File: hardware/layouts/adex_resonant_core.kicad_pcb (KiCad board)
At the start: 4 copper layers, 50 x 50 mm, 96 parts

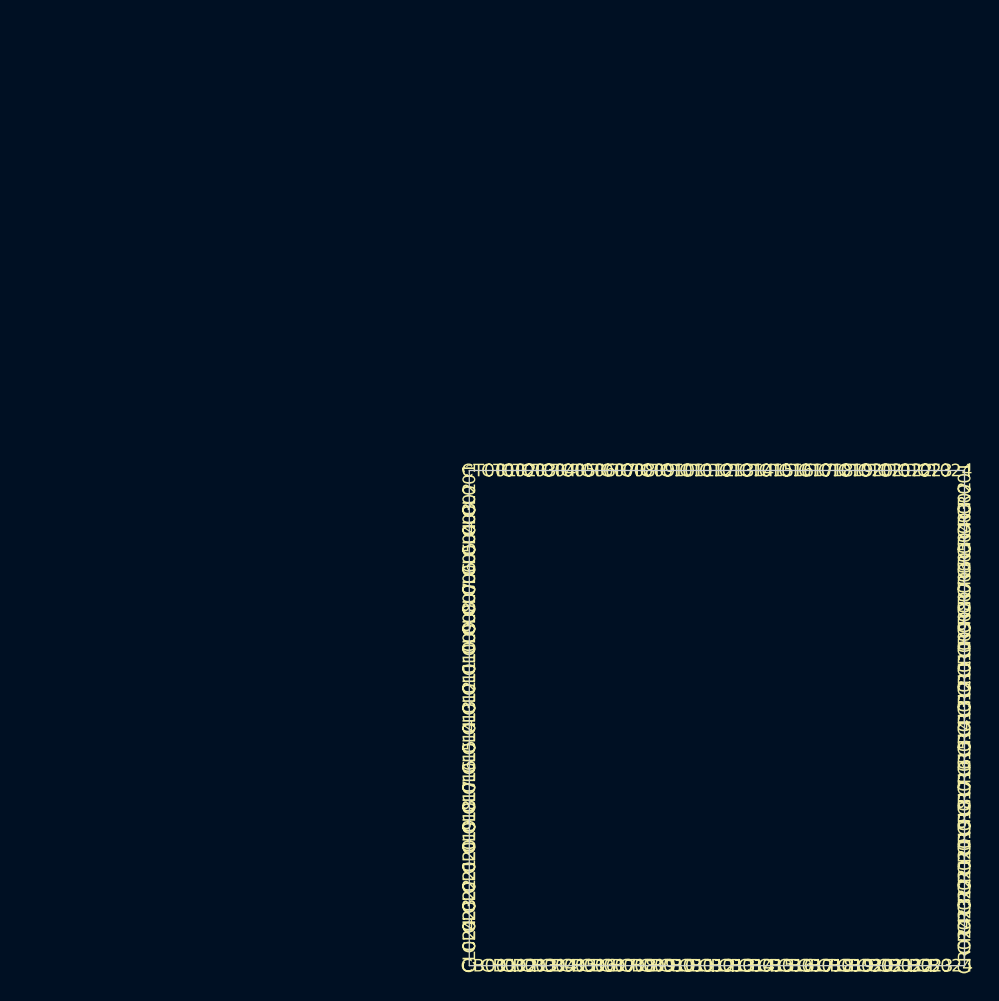
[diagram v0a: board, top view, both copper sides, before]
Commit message: fix(hardware): unpack stacked footprints to grid and set edge clearance to 0 for castellated pads
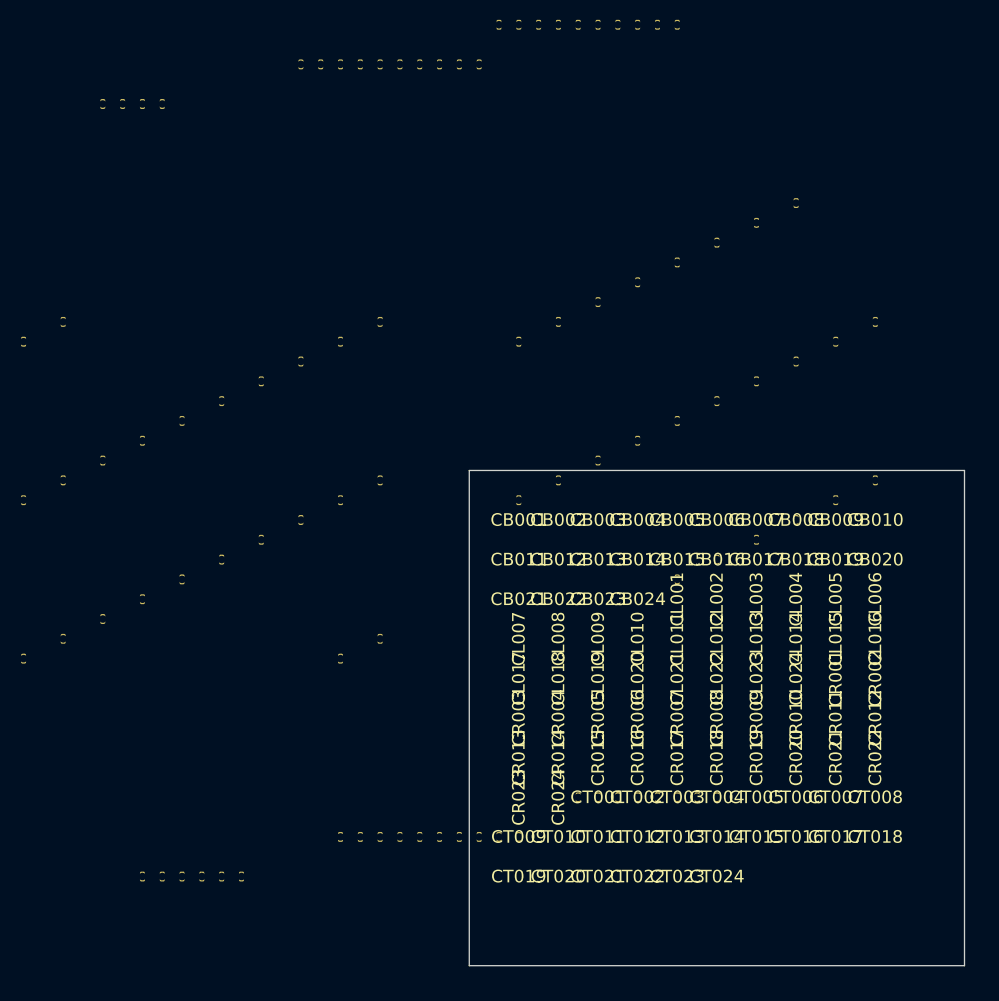
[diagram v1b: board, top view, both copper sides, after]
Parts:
- moved CT019 52.6 mm to (5.00, 41.0)
- moved CB021 52.3 mm to (5.00, 13.0)
- moved CT020 51.4 mm to (9.00, 41.0)
- moved CB022 50.9 mm to (9.00, 13.0)
- moved CT021 50.2 mm to (13.0, 41.0)
- moved CB010 49.7 mm to (41.0, 5.00)
- moved CB023 49.6 mm to (13.0, 13.0)
- moved CT022 49.1 mm to (17.0, 41.0)
- moved CB009 48.8 mm to (37.0, 5.00)
- moved CR003 48.8 mm to (5.00, 25.0)
- moved CB024 48.3 mm to (17.0, 13.0)
- moved CB008 48.1 mm to (33.0, 5.00)
- moved CT023 48.0 mm to (21.0, 41.0)
- moved CB007 47.4 mm to (29.0, 5.00)
- moved CT024 47.0 mm to (25.0, 41.0)
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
